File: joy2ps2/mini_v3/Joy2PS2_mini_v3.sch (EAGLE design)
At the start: 8 parts, among them IC1 ATMEGA168PROUND, Q1 BS170

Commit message: Add files via upload
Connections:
- net KB_DATA: now also Q1.S; no longer Q1.D
- net KB_DATA': now also Q1.D; no longer Q1.S
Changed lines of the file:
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@@
 </segment>
 <segment>
-<pinref part="Q1" gate="1" pin="D"/>
-<wire x1="-55.88" y1="109.22" x2="-35.56" y2="109.22" width="0.1524" layer="91"/>
-<label x="-38.1" y="109.22" size="1.778" layer="95"/>
+<pinref part="Q1" gate="1" pin="S"/>
+<wire x1="-55.88" y1="99.06" x2="-35.56" y2="99.06" width="0.1524" layer="91"/>
+<label x="-38.1" y="99.06" size="1.778" layer="95"/>
 </segment>
 </net>
@@
 <net name="KB_DATA'" class="0">
 <segment>
-<pinref part="Q1" gate="1" pin="S"/>
-<wire x1="-55.88" y1="99.06" x2="-35.56" y2="99.06" width="0.1524" layer="91"/>
-<label x="-38.1" y="99.06" size="1.778" layer="95"/>
-</segment>
-<segment>
 <pinref part="1" gate="A" pin="1"/>
 <wire x1="-55.88" y1="66.04" x2="-71.12" y2="66.04" width="0.1524" layer="91"/>
@@
 <label x="20.32" y="104.14" size="1.778" layer="95"/>
 </segment>
+<segment>
+<pinref part="Q1" gate="1" pin="D"/>
+<wire x1="-55.88" y1="109.22" x2="-35.56" y2="109.22" width="0.1524" layer="91"/>
+<label x="-38.1" y="109.22" size="1.778" layer="95"/>
+</segment>
 </net>

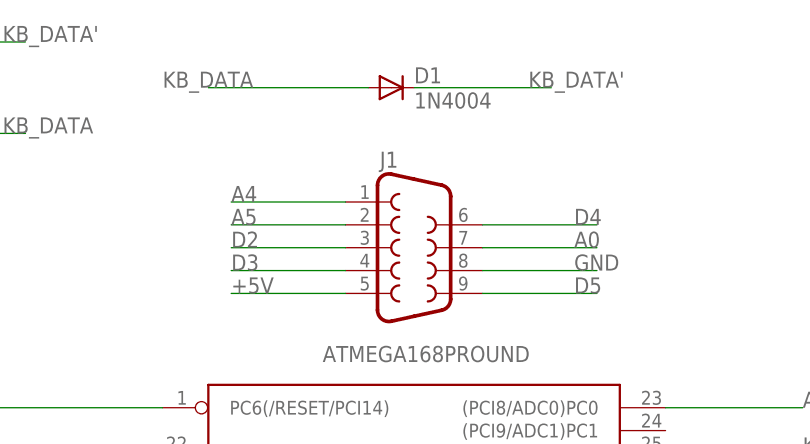
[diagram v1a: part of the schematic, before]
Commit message: Arcade version
Serigrafías para conexión tipo DB15 Neogeo
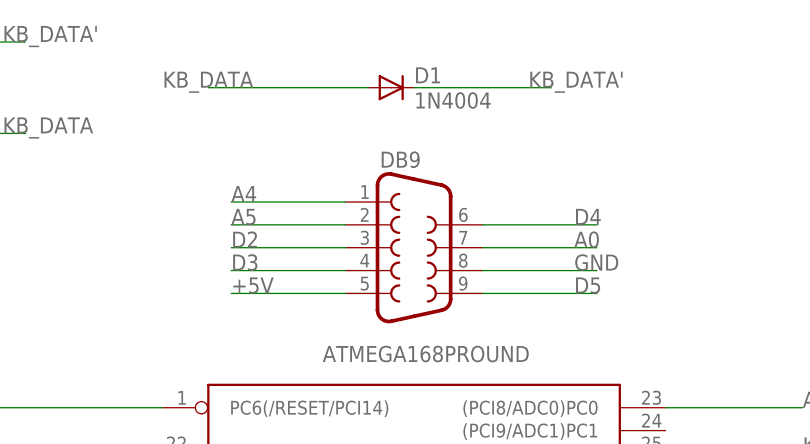
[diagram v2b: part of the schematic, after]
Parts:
- renumbered J1 to DB9
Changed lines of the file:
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@@
 <parts>
 <part name="_" library="GeekAmmo" deviceset="TACTILE-SWITCH" device="-PTH"/>
-<part name="J1" library="SparkFun-Connectors" deviceset="DB9" device="MALE"/>
+<part name="DB9" library="SparkFun-Connectors" deviceset="DB9" device="MALE"/>
 <part name="IC1" library="adafruit" deviceset="ATMEGA168*P" device="ROUND"/>
 <part name="1" library="pinhead" deviceset="PINHD-1X6" device=""/>
@@
 <instances>
 <instance part="_" gate="G$1" x="-63.5" y="83.82"/>
-<instance part="J1" gate="G$1" x="7.62" y="86.36"/>
+<instance part="DB9" gate="G$1" x="7.62" y="86.36"/>
 <instance part="IC1" gate="G$1" x="2.54" y="40.64"/>
 <instance part="1" gate="A" x="-53.34" y="58.42"/>
@@
 <net name="D2" class="0">
 <segment>
-<pinref part="J1" gate="G$1" pin="3"/>
+<pinref part="DB9" gate="G$1" pin="3"/>
 <wire x1="0" y1="86.36" x2="-12.7" y2="86.36" width="0.1524" layer="91"/>
 <label x="-12.7" y="86.36" size="1.778" layer="95"/>
@@
 <net name="D3" class="0">
 <segment>
-<pinref part="J1" gate="G$1" pin="4"/>
+<pinref part="DB9" gate="G$1" pin="4"/>
 <wire x1="0" y1="83.82" x2="-12.7" y2="83.82" width="0.1524" layer="91"/>
 <label x="-12.7" y="83.82" size="1.778" layer="95"/>
@@
 <net name="D4" class="0">
 <segment>
-<pinref part="J1" gate="G$1" pin="6"/>
+<pinref part="DB9" gate="G$1" pin="6"/>
 <wire x1="15.24" y1="88.9" x2="27.94" y2="88.9" width="0.1524" layer="91"/>
 <label x="25.4" y="88.9" size="1.778" layer="95"/>
@@
 <net name="D5" class="0">
 <segment>
-<pinref part="J1" gate="G$1" pin="9"/>
+<pinref part="DB9" gate="G$1" pin="9"/>
 <wire x1="15.24" y1="81.28" x2="27.94" y2="81.28" width="0.1524" layer="91"/>
 <label x="25.4" y="81.28" size="1.778" layer="95"/>
@@
 <net name="+5V" class="0">
 <segment>
-<pinref part="J1" gate="G$1" pin="5"/>
+<pinref part="DB9" gate="G$1" pin="5"/>
 <wire x1="0" y1="81.28" x2="-12.7" y2="81.28" width="0.1524" layer="91"/>
 <label x="-12.7" y="81.28" size="1.778" layer="95"/>
@@
 <net name="A5" class="0">
 <segment>
-<pinref part="J1" gate="G$1" pin="2"/>
+<pinref part="DB9" gate="G$1" pin="2"/>
 <wire x1="0" y1="88.9" x2="-12.7" y2="88.9" width="0.1524" layer="91"/>
 <label x="-12.7" y="88.9" size="1.778" layer="95"/>
@@
 <net name="A4" class="0">
 <segment>
-<pinref part="J1" gate="G$1" pin="1"/>
+<pinref part="DB9" gate="G$1" pin="1"/>
 <wire x1="0" y1="91.44" x2="-12.7" y2="91.44" width="0.1524" layer="91"/>
 <label x="-12.7" y="91.44" size="1.778" layer="95"/>
@@
 </segment>
 <segment>
-<pinref part="J1" gate="G$1" pin="8"/>
+<pinref part="DB9" gate="G$1" pin="8"/>
 <wire x1="15.24" y1="83.82" x2="27.94" y2="83.82" width="0.1524" layer="91"/>
 <label x="25.4" y="83.82" size="1.778" layer="95"/>
@@
 <net name="A0" class="0">
 <segment>
-<pinref part="J1" gate="G$1" pin="7"/>
+<pinref part="DB9" gate="G$1" pin="7"/>
 <wire x1="15.24" y1="86.36" x2="27.94" y2="86.36" width="0.1524" layer="91"/>
 <label x="25.4" y="86.36" size="1.778" layer="95"/>
